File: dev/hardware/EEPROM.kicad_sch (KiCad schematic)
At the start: 6 parts, among them U401 24LC256, U402 24LC256

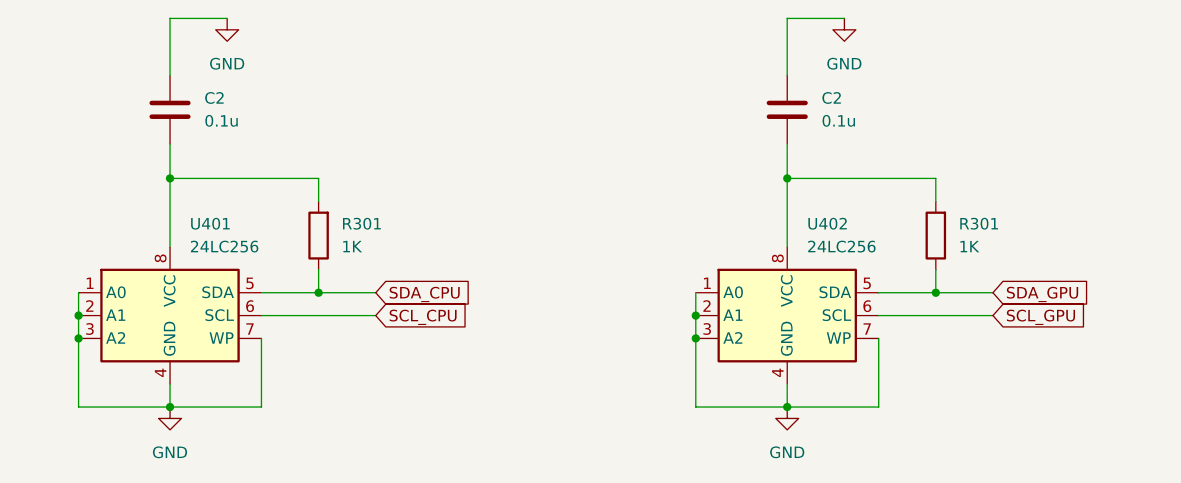
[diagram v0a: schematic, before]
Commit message: Finalized initial schematic
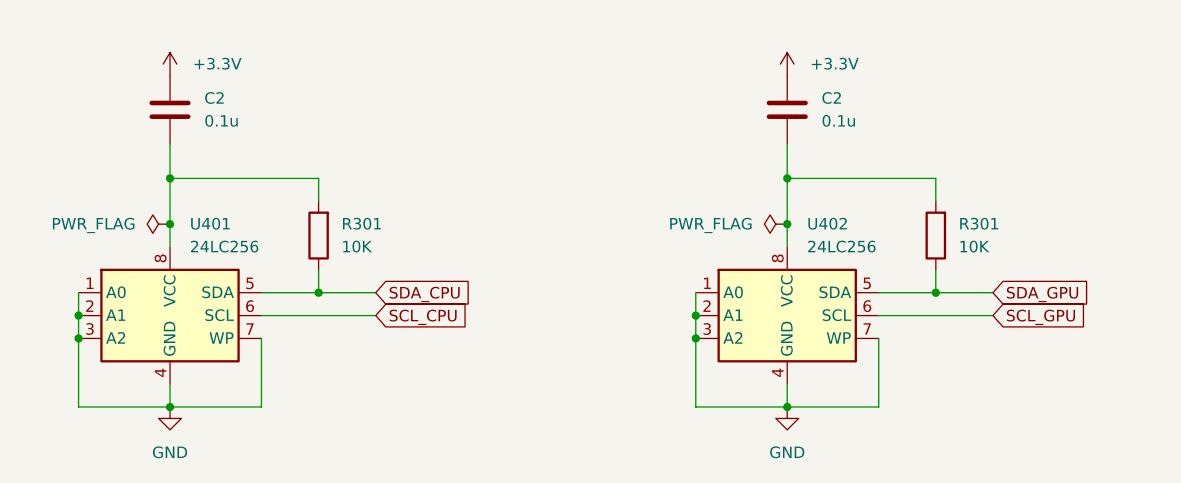
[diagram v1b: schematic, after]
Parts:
- R301: value 1K -> 10K
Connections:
- net GND: no longer C2.1, C2.1
- new net +3.3V: C2.1, C2.1
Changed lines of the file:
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@@
   (junction (at 161.29 101.6) (diameter 0) (color 0 0 0 0)
   )
+  (junction (at 171.45 91.44) (diameter 0) (color 0 0 0 0)
+  )
+  (junction (at 102.87 91.44) (diameter 0) (color 0 0 0 0)
+  )
+  (wire (pts (xy 171.45 91.44) (xy 171.45 93.98))
+    (stroke (width 0) (type default))
+  )
   (wire (pts (xy 102.87 86.36) (xy 119.38 86.36))
     (stroke (width 0) (type default))
@@
     (stroke (width 0) (type default))
   )
-  (wire (pts (xy 177.8 68.58) (xy 171.45 68.58))
-    (stroke (width 0) (type default))
-  )
   (wire (pts (xy 92.71 99.06) (xy 92.71 101.6))
     (stroke (width 0) (type default))
@@
     (stroke (width 0) (type default))
   )
-  (wire (pts (xy 102.87 86.36) (xy 102.87 93.98))
+  (wire (pts (xy 102.87 86.36) (xy 102.87 91.44))
     (stroke (width 0) (type default))
   )
@@
     (stroke (width 0) (type default))
   )
-  (wire (pts (xy 102.87 68.58) (xy 102.87 74.93))
-    (stroke (width 0) (type default))
-  )
   (wire (pts (xy 92.71 101.6) (xy 92.71 104.14))
     (stroke (width 0) (type default))
   )
-  (wire (pts (xy 171.45 86.36) (xy 171.45 93.98))
+  (wire (pts (xy 171.45 86.36) (xy 171.45 91.44))
     (stroke (width 0) (type default))
   )
@@
     (stroke (width 0) (type default))
   )
+  (wire (pts (xy 102.87 91.44) (xy 102.87 93.98))
+    (stroke (width 0) (type default))
+  )
   (wire (pts (xy 161.29 101.6) (xy 161.29 104.14))
     (stroke (width 0) (type default))
   )
-  (wire (pts (xy 171.45 68.58) (xy 171.45 74.93))
-    (stroke (width 0) (type default))
-  )
   (wire (pts (xy 181.61 111.76) (xy 171.45 111.76))
     (stroke (width 0) (type default))
@@
   )
   (wire (pts (xy 161.29 104.14) (xy 161.29 111.76))
-    (stroke (width 0) (type default))
-  )
-  (wire (pts (xy 109.22 68.58) (xy 102.87 68.58))
     (stroke (width 0) (type default))
   )
@@
     )
   )
+  (symbol (lib_id "power:+3.3V") (at 102.87 74.93 0) (unit 1)
+    (in_bom yes) (on_board yes) (dnp no) (fields_autoplaced)
+    (property "Reference" "#PWR0210" (at 102.87 78.74 0)
+      (effects (font (size 1.27 1.27)) hide)
+    )
+    (property "Value" "+3.3V" (at 105.41 73.66 0)
+      (effects (font (size 1.27 1.27)) (justify left))
+    )
+    (property "Footprint" "" (at 102.87 74.93 0)
+      (effects (font (size 1.27 1.27)) hide)
+    )
+    (property "Datasheet" "" (at 102.87 74.93 0)
+      (effects (font (size 1.27 1.27)) hide)
+    )
+    (pin "1")
+    (instances
+      (project "jcap"
+        (path "/7fc25e9e-3600-419b-89ef-b962e4e374c1/203ea849-2dbb-4e64-89c6-7fa05a05e11f"
+          (reference "#PWR0210") (unit 1)
+        )
+        (path "/7fc25e9e-3600-419b-89ef-b962e4e374c1/fef6ede6-5843-4140-8b23-7dcea4adc604"
+          (reference "#PWR0401") (unit 1)
+        )
+      )
+    )
+  )
   (symbol (lib_id "Device:R") (at 187.96 92.71 180) (unit 1)
     (in_bom yes) (on_board yes) (dnp no) (fields_autoplaced)
@@
       (effects (font (size 1.27 1.27)) (justify right))
     )
-    (property "Value" "1K" (at 190.5 93.98 0)
+    (property "Value" "10K" (at 190.5 93.98 0)
       (effects (font (size 1.27 1.27)) (justify right))
     )
@@
       (effects (font (size 1.27 1.27)) (justify right))
     )
-    (property "Value" "1K" (at 121.92 93.98 0)
+    (property "Value" "10K" (at 121.92 93.98 0)
       (effects (font (size 1.27 1.27)) (justify right))
     )
@@
     )
   )
-  (symbol (lib_id "power:GND") (at 109.22 68.58 0) (unit 1)
-    (in_bom yes) (on_board yes) (dnp no) (fields_autoplaced)
-    (property "Reference" "#PWR0401" (at 109.22 74.93 0)
-      (effects (font (size 1.27 1.27)) hide)
-    )
-    (property "Value" "GND" (at 109.22 73.66 0)
-      (effects (font (size 1.27 1.27)))
-    )
-    (property "Footprint" "" (at 109.22 68.58 0)
-      (effects (font (size 1.27 1.27)) hide)
-    )
-    (property "Datasheet" "" (at 109.22 68.58 0)
-      (effects (font (size 1.27 1.27)) hide)
-    )
-    (pin "1")
-    (instances
-      (project "jcap"
-        (path "/7fc25e9e-3600-419b-89ef-b962e4e374c1/fef6ede6-5843-4140-8b23-7dcea4adc604"
-          (reference "#PWR0401") (unit 1)
-        )
-      )
-    )
-  )
   (symbol (lib_id "Device:C") (at 102.87 78.74 0) (unit 1)
     (in_bom yes) (on_board yes) (dnp no) (fields_autoplaced)
@@
     )
   )
-  (symbol (lib_id "power:GND") (at 177.8 68.58 0) (unit 1)
-    (in_bom yes) (on_board yes) (dnp no) (fields_autoplaced)
-    (property "Reference" "#PWR0404" (at 177.8 74.93 0)
-      (effects (font (size 1.27 1.27)) hide)
-    )
-    (property "Value" "GND" (at 177.8 73.66 0)
-      (effects (font (size 1.27 1.27)))
-    )
-    (property "Footprint" "" (at 177.8 68.58 0)
-      (effects (font (size 1.27 1.27)) hide)
-    )
-    (property "Datasheet" "" (at 177.8 68.58 0)
-      (effects (font (size 1.27 1.27)) hide)
-    )
-    (pin "1")
-    (instances
-      (project "jcap"
+  (symbol (lib_id "power:+3.3V") (at 171.45 74.93 0) (unit 1)
+    (in_bom yes) (on_board yes) (dnp no) (fields_autoplaced)
+    (property "Reference" "#PWR0210" (at 171.45 78.74 0)
+      (effects (font (size 1.27 1.27)) hide)
+    )
+    (property "Value" "+3.3V" (at 173.99 73.66 0)
+      (effects (font (size 1.27 1.27)) (justify left))
+    )
+    (property "Footprint" "" (at 171.45 74.93 0)
+      (effects (font (size 1.27 1.27)) hide)
+    )
+    (property "Datasheet" "" (at 171.45 74.93 0)
+      (effects (font (size 1.27 1.27)) hide)
+    )
+    (pin "1")
+    (instances
+      (project "jcap"
+        (path "/7fc25e9e-3600-419b-89ef-b962e4e374c1/203ea849-2dbb-4e64-89c6-7fa05a05e11f"
+          (reference "#PWR0210") (unit 1)
+        )
         (path "/7fc25e9e-3600-419b-89ef-b962e4e374c1/fef6ede6-5843-4140-8b23-7dcea4adc604"
           (reference "#PWR0404") (unit 1)
         )
       )
+    )
+  )
+  (symbol (lib_id "power:PWR_FLAG") (at 171.45 91.44 90) (unit 1)
+    (in_bom yes) (on_board yes) (dnp no) (fields_autoplaced)
+    (property "Reference" "#FLG0302" (at 169.545 91.44 0)
+      (effects (font (size 1.27 1.27)) hide)
+    )
+    (property "Value" "PWR_FLAG" (at 167.64 91.44 90)
+      (effects (font (size 1.27 1.27)) (justify left))
+    )
+    (property "Footprint" "" (at 171.45 91.44 0)
+      (effects (font (size 1.27 1.27)) hide)
+    )
+    (property "Datasheet" "~" (at 171.45 91.44 0)
+      (effects (font (size 1.27 1.27)) hide)
+    )
+    (pin "1")
+    (instances
+      (project "jcap"
+        (path "/7fc25e9e-3600-419b-89ef-b962e4e374c1/f5a50cf1-3d87-469f-beb1-b0b9cfae00ce"
+          (reference "#FLG0302") (unit 1)
+        )
+        (path "/7fc25e9e-3600-419b-89ef-b962e4e374c1/203ea849-2dbb-4e64-89c6-7fa05a05e11f"
+          (reference "#FLG0201") (unit 1)
+        )
+        (path "/7fc25e9e-3600-419b-89ef-b962e4e374c1/fef6ede6-5843-4140-8b23-7dcea4adc604"
+          (reference "#FLG0401") (unit 1)
+        )
+      )
+    )
+  )
+  (symbol (lib_id "power:PWR_FLAG") (at 102.87 91.44 90) (unit 1)
+    (in_bom yes) (on_board yes) (dnp no) (fields_autoplaced)
+    (property "Reference" "#FLG0302" (at 100.965 91.44 0)
+      (effects (font (size 1.27 1.27)) hide)
+    )
+    (property "Value" "PWR_FLAG" (at 99.06 91.44 90)
+      (effects (font (size 1.27 1.27)) (justify left))
+    )
+    (property "Footprint" "" (at 102.87 91.44 0)
+      (effects (font (size 1.27 1.27)) hide)
+    )
+    (property "Datasheet" "~" (at 102.87 91.44 0)
+      (effects (font (size 1.27 1.27)) hide)
+    )
+    (pin "1")
+    (instances
+      (project "jcap"
+        (path "/7fc25e9e-3600-419b-89ef-b962e4e374c1/f5a50cf1-3d87-469f-beb1-b0b9cfae00ce"
+          (reference "#FLG0302") (unit 1)
+        )
+        (path "/7fc25e9e-3600-419b-89ef-b962e4e374c1/203ea849-2dbb-4e64-89c6-7fa05a05e11f"
+          (reference "#FLG0201") (unit 1)
+        )
+        (path "/7fc25e9e-3600-419b-89ef-b962e4e374c1/fef6ede6-5843-4140-8b23-7dcea4adc604"
+          (reference "#FLG0402") (unit 1)
+        )
+      )

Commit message: Started developing PCB layout
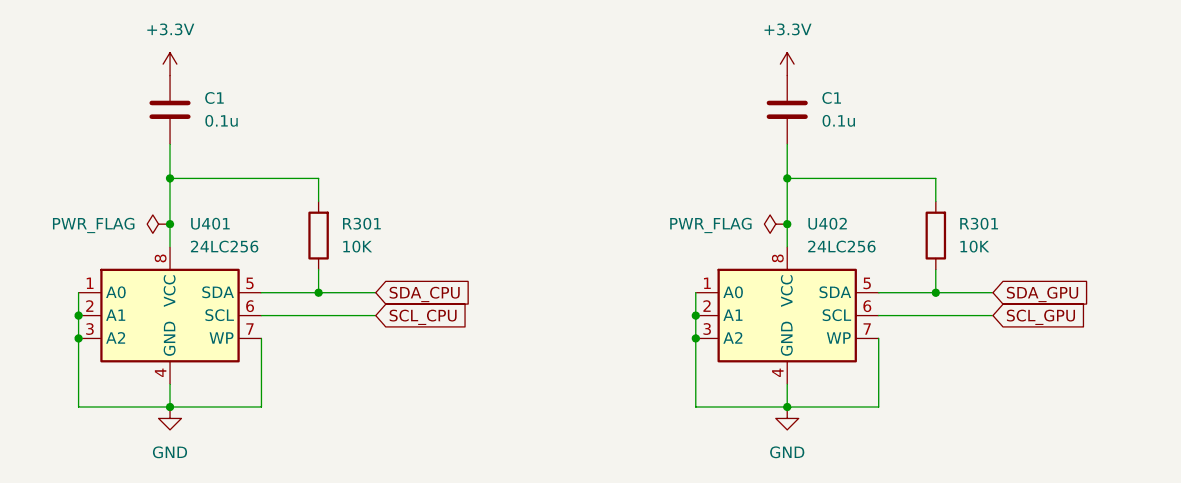
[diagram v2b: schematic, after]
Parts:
- removed C2 (x2): 0.1u, Capacitor_THT:C_Radial_D4.0mm_H7.0mm_P1.50mm, symbol Device:C
- added C1 (x2): 0.1u, Capacitor_THT:C_Disc_D3.4mm_W2.1mm_P2.50mm, symbol Device:C
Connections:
- net +3.3V: now also C1.2, C1.2
- net at R301.2, U402.8 (VCC): now also C1.1
- net at R301.2, U401.8 (VCC): now also C1.1
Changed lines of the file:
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@@
-    )
-  )
-  (symbol (lib_id "Device:C") (at 171.45 78.74 0) (unit 1)
-    (in_bom yes) (on_board yes) (dnp no) (fields_autoplaced)
-    (property "Reference" "C2" (at 175.26 77.47 0)
-      (effects (font (size 1.27 1.27)) (justify left))
-    )
-    (property "Value" "0.1u" (at 175.26 80.01 0)
-      (effects (font (size 1.27 1.27)) (justify left))
-    )
-    (property "Footprint" "Capacitor_THT:C_Radial_D4.0mm_H7.0mm_P1.50mm" (at 172.4152 82.55 0)
-      (effects (font (size 1.27 1.27)) hide)
-    )
-    (property "Datasheet" "~" (at 171.45 78.74 0)
-      (effects (font (size 1.27 1.27)) hide)
-    )
-    (pin "1")
-    (pin "2")
-    (instances
-      (project "jcap"
-        (path "/7fc25e9e-3600-419b-89ef-b962e4e374c1"
-          (reference "C2") (unit 1)
-        )
-        (path "/7fc25e9e-3600-419b-89ef-b962e4e374c1/203ea849-2dbb-4e64-89c6-7fa05a05e11f"
-          (reference "C2") (unit 1)
-        )
-        (path "/7fc25e9e-3600-419b-89ef-b962e4e374c1/f5a50cf1-3d87-469f-beb1-b0b9cfae00ce"
-          (reference "C302") (unit 1)
-        )
-        (path "/7fc25e9e-3600-419b-89ef-b962e4e374c1/fef6ede6-5843-4140-8b23-7dcea4adc604"
-          (reference "C402") (unit 1)
-        )
-      )
     )
   )
@@
       (effects (font (size 1.27 1.27)) hide)
     )
-    (property "Value" "+3.3V" (at 105.41 73.66 0)
-      (effects (font (size 1.27 1.27)) (justify left))
+    (property "Value" "+3.3V" (at 102.87 69.85 0)
+      (effects (font (size 1.27 1.27)))
     )
     (property "Footprint" "" (at 102.87 74.93 0)
@@
         (path "/7fc25e9e-3600-419b-89ef-b962e4e374c1/fef6ede6-5843-4140-8b23-7dcea4adc604"
           (reference "#PWR0402") (unit 1)
+        )
+      )
+    )
+  )
+  (symbol (lib_id "Device:C") (at 171.45 78.74 180) (unit 1)
+    (in_bom yes) (on_board yes) (dnp no) (fields_autoplaced)
+    (property "Reference" "C1" (at 175.26 77.47 0)
+      (effects (font (size 1.27 1.27)) (justify right))
+    )
+    (property "Value" "0.1u" (at 175.26 80.01 0)
+      (effects (font (size 1.27 1.27)) (justify right))
+    )
+    (property "Footprint" "Capacitor_THT:C_Disc_D3.4mm_W2.1mm_P2.50mm" (at 170.4848 74.93 0)
+      (effects (font (size 1.27 1.27)) hide)
+    )
+    (property "Datasheet" "~" (at 171.45 78.74 0)
+      (effects (font (size 1.27 1.27)) hide)
+    )
+    (pin "1")
+    (pin "2")
+    (instances
+      (project "jcap"
+        (path "/7fc25e9e-3600-419b-89ef-b962e4e374c1"
+          (reference "C1") (unit 1)
+        )
+        (path "/7fc25e9e-3600-419b-89ef-b962e4e374c1/203ea849-2dbb-4e64-89c6-7fa05a05e11f"
+          (reference "C1") (unit 1)
+        )
+        (path "/7fc25e9e-3600-419b-89ef-b962e4e374c1/fef6ede6-5843-4140-8b23-7dcea4adc604"
+          (reference "C402") (unit 1)
         )
       )
@@
     )
   )
-  (symbol (lib_id "Device:C") (at 102.87 78.74 0) (unit 1)
-    (in_bom yes) (on_board yes) (dnp no) (fields_autoplaced)
-    (property "Reference" "C2" (at 106.68 77.47 0)
-      (effects (font (size 1.27 1.27)) (justify left))
-    )
-    (property "Value" "0.1u" (at 106.68 80.01 0)
-      (effects (font (size 1.27 1.27)) (justify left))
-    )
-    (property "Footprint" "Capacitor_THT:C_Radial_D4.0mm_H7.0mm_P1.50mm" (at 103.8352 82.55 0)
-      (effects (font (size 1.27 1.27)) hide)
-    )
-    (property "Datasheet" "~" (at 102.87 78.74 0)
-      (effects (font (size 1.27 1.27)) hide)
-    )
-    (pin "1")
-    (pin "2")
-    (instances
-      (project "jcap"
-        (path "/7fc25e9e-3600-419b-89ef-b962e4e374c1"
-          (reference "C2") (unit 1)
-        )
-        (path "/7fc25e9e-3600-419b-89ef-b962e4e374c1/203ea849-2dbb-4e64-89c6-7fa05a05e11f"
-          (reference "C2") (unit 1)
-        )
-        (path "/7fc25e9e-3600-419b-89ef-b962e4e374c1/f5a50cf1-3d87-469f-beb1-b0b9cfae00ce"
-          (reference "C302") (unit 1)
-        )
-        (path "/7fc25e9e-3600-419b-89ef-b962e4e374c1/fef6ede6-5843-4140-8b23-7dcea4adc604"
-          (reference "C401") (unit 1)
-        )
-      )
-    )
-  )
   (symbol (lib_id "power:+3.3V") (at 171.45 74.93 0) (unit 1)
     (in_bom yes) (on_board yes) (dnp no) (fields_autoplaced)
@@
       (effects (font (size 1.27 1.27)) hide)
     )
-    (property "Value" "+3.3V" (at 173.99 73.66 0)
-      (effects (font (size 1.27 1.27)) (justify left))
+    (property "Value" "+3.3V" (at 171.45 69.85 0)
+      (effects (font (size 1.27 1.27)))
     )
     (property "Footprint" "" (at 171.45 74.93 0)
@@
         )
       )
+    )
+  )
+  (symbol (lib_id "Device:C") (at 102.87 78.74 180) (unit 1)
+    (in_bom yes) (on_board yes) (dnp no) (fields_autoplaced)
+    (property "Reference" "C1" (at 106.68 77.47 0)
+      (effects (font (size 1.27 1.27)) (justify right))
+    )
+    (property "Value" "0.1u" (at 106.68 80.01 0)
+      (effects (font (size 1.27 1.27)) (justify right))
+    )
+    (property "Footprint" "Capacitor_THT:C_Disc_D3.4mm_W2.1mm_P2.50mm" (at 101.9048 74.93 0)
+      (effects (font (size 1.27 1.27)) hide)
+    )
+    (property "Datasheet" "~" (at 102.87 78.74 0)
+      (effects (font (size 1.27 1.27)) hide)
+    )
+    (pin "1")
+    (pin "2")
+    (instances
+      (project "jcap"
+        (path "/7fc25e9e-3600-419b-89ef-b962e4e374c1"
+          (reference "C1") (unit 1)
+        )
+        (path "/7fc25e9e-3600-419b-89ef-b962e4e374c1/203ea849-2dbb-4e64-89c6-7fa05a05e11f"
+          (reference "C1") (unit 1)
+        )
+        (path "/7fc25e9e-3600-419b-89ef-b962e4e374c1/fef6ede6-5843-4140-8b23-7dcea4adc604"
+          (reference "C401") (unit 1)
+        )
+      )

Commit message: Finalized review schematic & pcb
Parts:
- removed C1 (x2): 0.1u, Capacitor_THT:C_Disc_D3.4mm_W2.1mm_P2.50mm, symbol Device:C
- added C1 (x2): 0.1u, Capacitor_THT:C_Disc_D3.4mm_W2.1mm_P2.50mm, symbol Device:C
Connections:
- net +3.3V: now also R301.2, R301.2, U401.8 (VCC), U402.8 (VCC), C1.2, C1.2
- net GND: now also C1.1, C1.1
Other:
- moved on the sheet: R301
